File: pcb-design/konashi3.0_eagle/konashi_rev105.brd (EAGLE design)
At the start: 33 x 52 mm, 37 parts, among them CN1 ZX62-B-5PA(11), CN2 S2B-PH-K-S, CN3 WML-C69, CN4 2X07, CN7 BK-913, IC1 LP2981-30DBVR, IC2 ZLDO1117G50DITR-ND

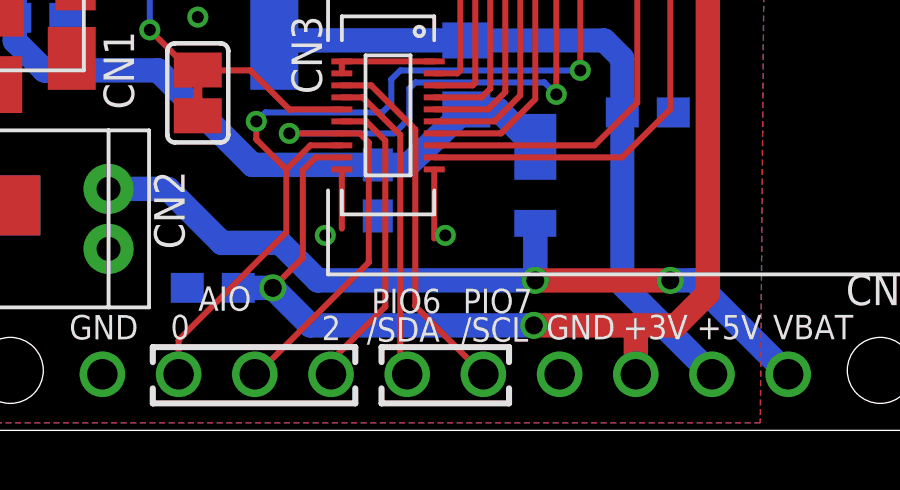
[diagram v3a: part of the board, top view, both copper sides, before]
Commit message: ガーバーデータ追加、レギュレータ型番変更
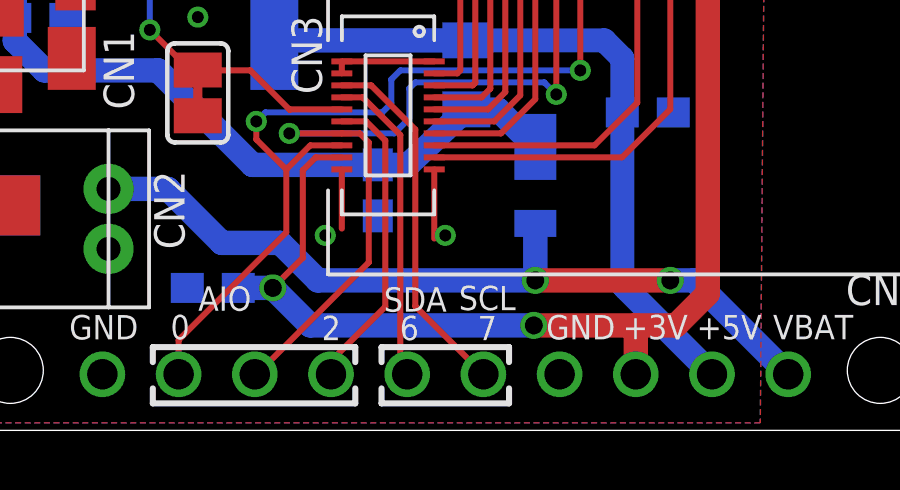
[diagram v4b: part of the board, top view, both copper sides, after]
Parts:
- C1: value 10u -> 2.2u
- C3: value 0.1u -> 1u
- IC1: value LP2981-30DBVR -> LP2985N
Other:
- board text added: "6"
- board text added: "7"
- board text added: "SCL"
- board text added: "SDA"
- board text removed: "/SCL"
- board text removed: "/SDA"
- board text removed: "PIO6"
- board text removed: "PIO7"
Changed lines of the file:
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@@
 <layer number="20" name="Dimension" color="15" fill="1" visible="yes" active="yes"/>
 <layer number="21" name="tPlace" color="16" fill="1" visible="yes" active="yes"/>
-<layer number="22" name="bPlace" color="17" fill="1" visible="no" active="yes"/>
-<layer number="23" name="tOrigins" color="16" fill="1" visible="no" active="yes"/>
+<layer number="22" name="bPlace" color="17" fill="1" visible="yes" active="yes"/>
+<layer number="23" name="tOrigins" color="16" fill="1" visible="yes" active="yes"/>
 <layer number="24" name="bOrigins" color="17" fill="1" visible="yes" active="yes"/>
 <layer number="25" name="tNames" color="16" fill="1" visible="yes" active="yes"/>
@@
 <rectangle x1="30" y1="45.5" x2="32" y2="47.5" layer="1"/>
 <rectangle x1="30" y1="45.5" x2="32" y2="47.5" layer="16"/>
-<text x="15.2" y="4.72" size="0.8128" layer="21" font="vector" rot="R180" align="bottom-center">PIO6</text>
-<text x="18.15" y="3.77" size="0.8128" layer="21" font="vector" rot="R180" align="bottom-center">/SCL</text>
-<text x="14.9" y="3.82" size="0.8128" layer="22" font="vector" rot="MR180" align="bottom-center">/SDA</text>
-<text x="17.8" y="3.82" size="0.8128" layer="22" font="vector" rot="MR180" align="bottom-center">/SCL</text>
-<text x="15.1" y="3.77" size="0.8128" layer="21" font="vector" rot="R180" align="bottom-center">/SDA</text>
-<text x="18.25" y="4.72" size="0.8128" layer="21" font="vector" rot="R180" align="bottom-center">PIO7</text>
-<text x="14.9" y="4.82" size="0.8128" layer="22" font="vector" rot="MR180" align="bottom-center">PIO6</text>
-<text x="17.8" y="4.82" size="0.8128" layer="22" font="vector" rot="MR180" align="bottom-center">PIO7</text>
+<text x="15.3" y="3.82" size="0.8128" layer="21" font="vector" rot="R180" align="bottom-center">6</text>
+<text x="17.9" y="4.82" size="0.8128" layer="21" font="vector" rot="R180" align="bottom-center">SCL</text>
+<text x="15.3" y="4.82" size="0.8128" layer="22" font="vector" rot="MR180" align="bottom-center">SDA</text>
+<text x="17.7" y="4.82" size="0.8128" layer="22" font="vector" rot="MR180" align="bottom-center">SCL</text>
+<text x="15.5" y="4.77" size="0.8128" layer="21" font="vector" rot="R180" align="bottom-center">SDA</text>
+<text x="17.9" y="3.82" size="0.8128" layer="21" font="vector" rot="R180" align="bottom-center">7</text>
+<text x="15.1" y="3.82" size="0.8128" layer="22" font="vector" rot="MR180" align="bottom-center">6</text>
+<text x="17.65" y="3.82" size="0.8128" layer="22" font="vector" rot="MR180" align="bottom-center">7</text>
 <text x="18.3" y="21.8" size="0.8128" layer="25">(0)</text>
 <text x="15.8" y="21.8" size="0.8128" layer="25">(1)</text>
@@
 <attribute name="NAME" x="28.165" y="21.065" size="0.8128" layer="26" font="vector" rot="MR180"/>
 </element>
-<element name="C1" library="rcl" package="C0603" value="10u" x="4.44" y="25.9" smashed="yes" rot="MR90">
+<element name="C1" library="rcl" package="C0603" value="2.2u" x="4.44" y="25.9" smashed="yes" rot="MR90">
 <attribute name="NAME" x="5.375" y="25.365" size="0.8128" layer="26" font="vector" rot="MR90"/>
 </element>
-<element name="C3" library="rcl" package="C0603" value="0.1u" x="3" y="13.75" smashed="yes" rot="MR180">
+<element name="C3" library="rcl" package="C0603" value="1u" x="3" y="13.75" smashed="yes" rot="MR180">
 <attribute name="NAME" x="2.165" y="13.015" size="0.8128" layer="26" font="vector" rot="MR180"/>
 </element>
@@
 <element name="U$13" library="konashilogo" package="KONASHI_LOGO_WIRE" value="" x="16" y="40.1" rot="MR0"/>
 <element name="U$14" library="yukailib" package="YUKAILOGO" value="" x="16.5" y="31.1" rot="MR0"/>
-<element name="IC1" library="LDO" package="SOT-23" value="LP2981-30DBVR" x="2.4" y="21.7" smashed="yes" rot="MR0">
+<element name="IC1" library="LDO" package="SOT-23" value="LP2985N" x="2.4" y="21.7" smashed="yes" rot="MR0">
 <attribute name="NAME" x="5.31" y="22.77" size="0.8128" layer="26" font="vector" rot="MR270"/>
 </element>

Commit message: BOM追加
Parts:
- IC1: value LP2985N -> LP2985IM5-3.6
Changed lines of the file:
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@@
 <element name="U$13" library="konashilogo" package="KONASHI_LOGO_WIRE" value="" x="16" y="40.1" rot="MR0"/>
 <element name="U$14" library="yukailib" package="YUKAILOGO" value="" x="16.5" y="31.1" rot="MR0"/>
-<element name="IC1" library="LDO" package="SOT-23" value="LP2985N" x="2.4" y="21.7" smashed="yes" rot="MR0">
+<element name="IC1" library="LDO" package="SOT-23" value="LP2985IM5-3.6" x="2.4" y="21.7" smashed="yes" rot="MR0">
 <attribute name="NAME" x="5.31" y="22.77" size="0.8128" layer="26" font="vector" rot="MR270"/>
 </element>
@@
 </signal>
 </signals>
-<errors>
-</errors>
 </board>
 </drawing>
